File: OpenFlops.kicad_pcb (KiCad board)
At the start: 2 copper layers, 111.6 x 59.4 mm, 87 parts, among them J99 OSHW_LOGO, P1 FLOPPY_CONN, P2 POWER_INPUT, P3 USB_A_FEMALE, P4 PROG_PORT, P5 JUMPER_JC, P6 ENCODER_PORT, P7 DISPLAY_PORT, P8 USB_HEADER, P9 EXTERNAL_SPEAKER, Q1 BSS138, Q2 BSS138, Q3 BSS138, Q4 BSS138, Q5 BSS138, Q6 BSS138, Q7 MMBT3904, U1 74HCT04, U3 STM32F105RBT6, U4 LM1117-3.3, Y1 8 MHz

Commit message: updated to kicad 6; dual mount smt/tht crystal; added test points for swd
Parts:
- added TP2: SWDIO, TestPoint:TestPoint_Pad_D1.0mm, F.Cu at (173.6, 70.9)
- added TP3: SWCLK, TestPoint:TestPoint_Pad_D1.0mm, F.Cu at (173.6, 68.7)
- Y1: footprint Crystal:Crystal_HC49-U_Vertical -> OpenFlops:Crystal_HC49-DualType
- moved Y1 1.97 mm to (154.5, 70.2)
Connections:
- net /~dskchg renamed /~{dskchg}
- net /~dskchg_3v3 renamed /~{dskchg_3v3}
- net /~index renamed /~{index}
- net /~index_3v3 renamed /~{index_3v3}
- net /~inuse renamed /~{inuse}
- net /~mtron renamed /~{mtron}
- net /~rdata renamed /~{rdata}
- net /~rdata_3v3 renamed /~{rdata_3v3}
- net /~rdy renamed /~{rdy}
- net /~rdy_3v3 renamed /~{rdy_3v3}
- net /~sel0 renamed /~{sel0}
- net /~sel1 renamed /~{sel1}
- net /~sel2 renamed /~{sel2}
- net /~selx renamed /~{selx}
- net /~sely renamed /~{sely}
- net /~side renamed /~{side}
- net /~trk0_3v3 renamed /~{trk0_3v3}
- net /~wprot renamed /~{wprot}
- net /~wprot_3v3 renamed /~{wprot_3v3}
- P1 pad 20: /~step -> /dir
- P1 pad 22: /~wdata -> /dir
- P1 pad 24: /~wgate -> /dir
- P1 pad 26: /~trk0 -> /dir
- P1 pad 6: (no net) -> /~{sel3}
- P2 pad 4: (no net) -> unconnected-(P2-Pad4)
- PU6 pad 2: /~step -> /dir
- PU7 pad 2: /~wdata -> /dir
- PU8 pad 2: /~wgate -> /dir
- PU9 pad 2: /~trk0 -> /dir
- Q2 pad 3: /~trk0 -> /dir
- U3 pad 10: (no net) -> unconnected-(U3-Pad10)
- U3 pad 11: (no net) -> unconnected-(U3-Pad11)
- U3 pad 15: /~step -> /dir
- U3 pad 20: (no net) -> unconnected-(U3-Pad20)
- U3 pad 21: (no net) -> unconnected-(U3-Pad21)
- U3 pad 22: (no net) -> unconnected-(U3-Pad22)
- U3 pad 24: (no net) -> unconnected-(U3-Pad24)
- U3 pad 25: (no net) -> unconnected-(U3-Pad25)
- U3 pad 33: (no net) -> /spi_cs
- U3 pad 34: (no net) -> /spi_clk
- U3 pad 35: (no net) -> /spi_do
- U3 pad 36: (no net) -> /spi_di
- U3 pad 40: (no net) -> unconnected-(U3-Pad40)
- U3 pad 41: /~wdata -> /dir
- U3 pad 46: (no net) -> /swdio
- U3 pad 49: (no net) -> /swclk
- U3 pad 54: (no net) -> unconnected-(U3-Pad54)
- U3 pad 62: /~wgate -> /dir
- U3 pad 8: (no net) -> unconnected-(U3-Pad8)
- U3 pad 9: (no net) -> unconnected-(U3-Pad9)
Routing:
- net /dir: track 86.6 -> 436.0 mm, vias 2 -> 7
- net /~wgate: track 106.8 -> 0.00 mm, vias 1 -> 0
- net /~wdata: track 104.9 -> 0.00 mm, vias 1 -> 0
- net /~step: track 78.5 -> 0.00 mm, vias 2 -> 0
- net /~trk0: track 59.3 -> 0.00 mm, vias 1 -> 0
- net /swdio: track 0.00 -> 7.64 mm
- net /swclk: track 0.00 -> 5.27 mm
- net GND: track 0.00 -> 1.52 mm
- net Net-(C5-Pad1): track 15.4 -> 14.5 mm
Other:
- net class Default removed
- net class Power removed
- net class uC removed
- board text added: "SWCLK"
- board text added: "SWDIO"
- board text added: "provided by silvestron.com"

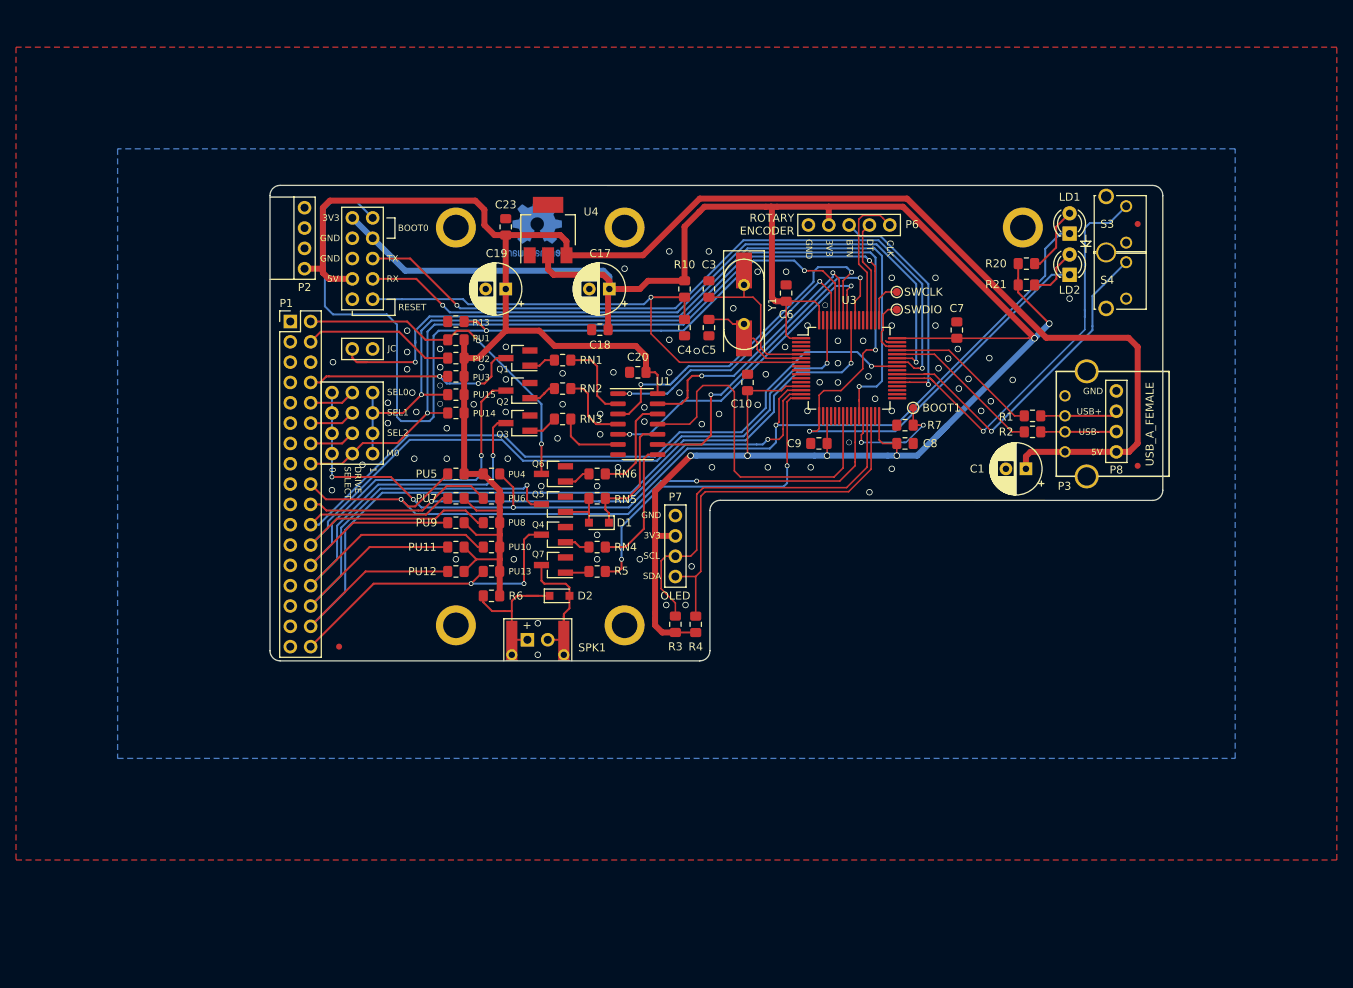
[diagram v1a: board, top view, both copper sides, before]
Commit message: update for citizen w1d
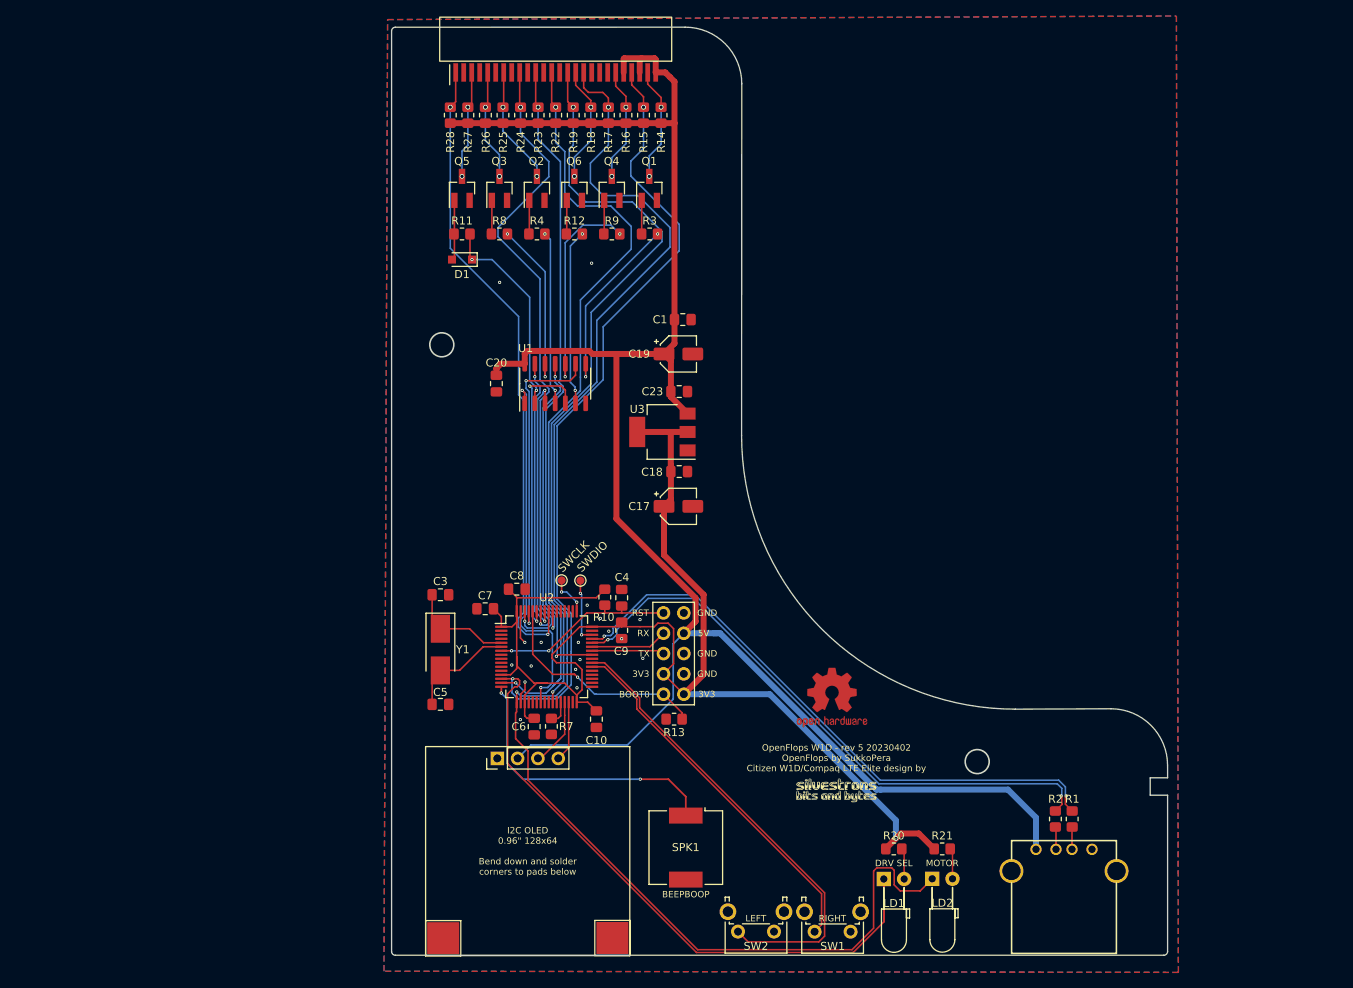
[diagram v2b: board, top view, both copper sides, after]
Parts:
- removed D2: 1N4148, Diode_SMD:D_SOD-323_HandSoldering
- removed FID1, FID2, FID3: Fiducial, Fiducial:Fiducial_0.75mm_Mask1.5mm
- removed H1, H2, H3, H4, H5: MountingHole_Pad, OpenFlops:MountingHole_M3_Pad
- removed P1: FLOPPY_CONN, Connector_PinHeader_2.54mm:PinHeader_2x17_P2.54mm_Vertical
- removed P2: POWER_INPUT, OpenFlops:PinHeader_1x04_P2.54mm_Vertical
- removed P3: USB_A_FEMALE, OpenFlops:USB_A_FEMALE
- removed P4: PROG_PORT, OpenFlops:PinHeader_2x05_P2.54mm_Vertical
- removed P5: JUMPER_JC, OpenFlops:PinHeader_1x02_P2.54mm_Vertical
- removed P6: ENCODER_PORT, OpenFlops:PinHeader_1x05_P2.54mm_Vertical
- removed P7: DISPLAY_PORT, OpenFlops:PinHeader_1x04_P2.54mm_Vertical
- removed P8: USB_HEADER, OpenFlops:PinHeader_1x04_P2.54mm_Vertical
- removed P9: EXTERNAL_SPEAKER, OpenFlops:PinHeader_1x02_P2.54mm_Mute
- removed PA5, PB5, PC5, PD5: Conn_01x03, OpenFlops:PinHeader_1x03_P2.54mm_Mute
- removed PU1, PU10, PU11, PU12, PU13, PU14, PU15, PU2, PU3, PU4, PU5, PU6, PU7, PU8, PU9: 1k, Resistor_SMD:R_0805_2012Metric_Pad1.15x1.40mm_HandSolder
- removed Q7: MMBT3904, Package_TO_SOT_SMD:SOT-23_Handsoldering
- removed R5, RN1, RN2, RN3, RN4, RN5, RN6: 1K, Resistor_SMD:R_0805_2012Metric_Pad1.15x1.40mm_HandSolder
- removed R6: 22, Resistor_SMD:R_0805_2012Metric_Pad1.15x1.40mm_HandSolder
- removed S3: BT_RIGHT, OpenFlops:PUSH_BUTTON_RIGHT_ANGLE
- removed S4: BT_LEFT, OpenFlops:PUSH_BUTTON_RIGHT_ANGLE
- removed TP1: BOOT1, TestPoint:TestPoint_Pad_D1.0mm
- removed U4: LM1117-3.3, Package_TO_SOT_SMD:SOT-223-3_TabPin2
- added J1: FDD, Silvestron Components:Adam_Tech_PCB-C5-26-SA-SMT_1x26_P1.00mm_Horizontal, F.Cu at (131.0, 40.3)
- added J2: USB_A_FEMALE, OpenFlops:USB_A_FEMALE, F.Cu at (194.5, 144.9)
- added J3: PROG_PORT, OpenFlops:PinHeader_2x05_P2.54mm_Vertical, F.Cu at (144.4, 108.8)
- added J4: OLED, Connector_PinHeader_2.54mm:PinHeader_1x04_P2.54mm_Vertical, F.Cu at (123.7, 127.0)
- added J5: OLED Mount, TestPoint:TestPoint_Pad_4.0x4.0mm, F.Cu at (116.9, 149.5)
- added J6: OLED Mount, TestPoint:TestPoint_Pad_4.0x4.0mm, F.Cu at (138.1, 149.4)
- added J7: SBAB_LOGO, Silvestron Components:sbab-tiny-logo, F.Cu at (166.1, 131.0)
- added R11: 1k, Resistor_SMD:R_0805_2012Metric_Pad1.20x1.40mm_HandSolder, F.Cu at (119.3, 61.4)
- added R12: 1k, Resistor_SMD:R_0805_2012Metric_Pad1.20x1.40mm_HandSolder, F.Cu at (133.3, 61.4)
- added R14: 1k, Resistor_SMD:R_0805_2012Metric_Pad1.20x1.40mm_HandSolder, F.Cu at (144.1, 46.6)
- added R15: 1k, Resistor_SMD:R_0805_2012Metric_Pad1.20x1.40mm_HandSolder, F.Cu at (141.9, 46.6)
- added R16: 1k, Resistor_SMD:R_0805_2012Metric_Pad1.20x1.40mm_HandSolder, F.Cu at (139.7, 46.6)
- added R17: 1k, Resistor_SMD:R_0805_2012Metric_Pad1.20x1.40mm_HandSolder, F.Cu at (137.5, 46.6)
- added R18: 1k, Resistor_SMD:R_0805_2012Metric_Pad1.20x1.40mm_HandSolder, F.Cu at (135.4, 46.6)
- added R19: 1k, Resistor_SMD:R_0805_2012Metric_Pad1.20x1.40mm_HandSolder, F.Cu at (133.2, 46.6)
- added R22: 1k, Resistor_SMD:R_0805_2012Metric_Pad1.20x1.40mm_HandSolder, F.Cu at (131.0, 46.6)
- added R23: 1k, Resistor_SMD:R_0805_2012Metric_Pad1.20x1.40mm_HandSolder, F.Cu at (128.8, 46.6)
- added R24: 1k, Resistor_SMD:R_0805_2012Metric_Pad1.20x1.40mm_HandSolder, F.Cu at (126.6, 46.6)
- added R25: 1k, Resistor_SMD:R_0805_2012Metric_Pad1.20x1.40mm_HandSolder, F.Cu at (124.4, 46.6)
- added R26: 1k, Resistor_SMD:R_0805_2012Metric_Pad1.20x1.40mm_HandSolder, F.Cu at (122.2, 46.6)
- added R27: 1k, Resistor_SMD:R_0805_2012Metric_Pad1.20x1.40mm_HandSolder, F.Cu at (120.0, 46.6)
- added R28: 1k, Resistor_SMD:R_0805_2012Metric_Pad1.20x1.40mm_HandSolder, F.Cu at (117.8, 46.6)
- added R8: 1k, Resistor_SMD:R_0805_2012Metric_Pad1.20x1.40mm_HandSolder, F.Cu at (123.9, 61.4)
- added R9: 1k, Resistor_SMD:R_0805_2012Metric_Pad1.20x1.40mm_HandSolder, F.Cu at (138.0, 61.4)
- added SW1: BT_RIGHT, Button_Switch_THT:SW_Tactile_SPST_Angled_PTS645Vx83-2LFS, F.Cu at (167.8, 148.7)
- added SW2: BT_LEFT, Button_Switch_THT:SW_Tactile_SPST_Angled_PTS645Vx83-2LFS, F.Cu at (158.2, 148.7)
- added U2: STM32F105RBT6, Package_QFP:LQFP-64_10x10mm_P0.5mm, F.Cu at (129.8, 114.3)
- C1: value 100u -> 10u; footprint Capacitor_THT:CP_Radial_D6.3mm_P2.50mm -> Capacitor_SMD:C_0805_2012Metric_Pad1.18x1.45mm_HandSolder
- C10, C18, C20, C23, C4, C6, C7, C8, C9: footprint Capacitor_SMD:C_0805_2012Metric_Pad1.15x1.40mm_HandSolder -> Capacitor_SMD:C_0805_2012Metric_Pad1.18x1.45mm_HandSolder
- C17, C19: footprint Capacitor_THT:CP_Radial_D6.3mm_P2.50mm -> Capacitor_SMD:CP_Elec_4x5.4
- C3, C5: value 22p -> 20p; footprint Capacitor_SMD:C_0805_2012Metric_Pad1.15x1.40mm_HandSolder -> Capacitor_SMD:C_0805_2012Metric_Pad1.18x1.45mm_HandSolder
- J99: moved to F.Cu
- LD1, LD2: footprint LED_THT:LED_D3.0mm -> LED_THT:LED_D3.0mm_Horizontal_O3.81mm_Z6.0mm
- R1, R10, R13, R2, R20, R21, R7: footprint Resistor_SMD:R_0805_2012Metric_Pad1.15x1.40mm_HandSolder -> Resistor_SMD:R_0805_2012Metric_Pad1.20x1.40mm_HandSolder
- R3, R4: value 3.3K -> 1k; footprint Resistor_SMD:R_0805_2012Metric_Pad1.15x1.40mm_HandSolder -> Resistor_SMD:R_0805_2012Metric_Pad1.20x1.40mm_HandSolder
- SPK1: footprint OpenFlops:Buzzer -> Buzzer_Beeper:Buzzer_CUI_CPT-9019S-SMT
- U3: value STM32F105RBT6 -> LM1117-3.3; footprint OpenFlops:LQFP-64_Handsoldering -> Package_TO_SOT_SMD:SOT-223-3_TabPin2
- Y1: footprint OpenFlops:Crystal_HC49-DualType -> Crystal:Crystal_SMD_5032-2Pin_5.0x3.2mm_HandSoldering
- moved LD1 83.9 mm to (172.0, 142.1), turned to 0 degrees
- moved LD2 77.4 mm to (178.0, 142.1), turned to 0 degrees
- moved R20 75.0 mm to (173.2, 138.3)
- moved R21 71.3 mm to (179.3, 138.3)
- moved J99 69.2 mm to (165.5, 119.4), turned to 0 degrees
- moved C7 68.5 mm to (122.1, 108.3), turned to 180 degrees
- moved C6 62.7 mm to (128.3, 123.0), turned to -90 degrees
- moved R7 58.1 mm to (130.4, 123.0), turned to 90 degrees
- moved C5 57.8 mm to (116.5, 120.2), turned to 0 degrees
- moved Y1 57.5 mm to (116.5, 113.4)
- moved R13 56.7 mm to (145.8, 122.1)
- moved TP3 55.3 mm to (131.7, 104.8)
- moved R4 52.7 mm to (128.6, 61.4), turned to 0 degrees
- moved TP2 52.1 mm to (134.1, 104.8)
- moved C8 51.8 mm to (126.1, 105.8)
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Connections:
- LD1 pad 1: /~{selx} -> /~{drvs}
- LD2 pad 1: /~{sely} -> /~{mote}
- Q2 pad 3: /dir -> /~{trk00}
- Q3 pad 3: /~{wprot} -> /~{wpt}
- Q4 pad 3: /~{rdy} -> /~{dskchg}
- Q6 pad 3: /~{dskchg} -> /~{redwc}
- R3 pad 1: +3V3 -> Net-(Q1-Pad1)
- R3 pad 2: /disp_clk -> Net-(R3-Pad2)
- R4 pad 1: +3V3 -> Net-(Q2-Pad1)
- R4 pad 2: /disp_dio -> Net-(R4-Pad2)
- SPK1 pad 1: /spk+ -> /jb
- SPK1 pad 2: /spk- -> GND
- U1 pad 1: /~{index_3v3} -> /~{rdata_3v3}
- U1 pad 10: Net-(D1-Pad1) -> Net-(R9-Pad2)
- U1 pad 11: /~{rdata_3v3} -> /~{dskchg_3v3}
- U1 pad 13: /~{dskchg_3v3} -> /~{wprot_3v3}
- U1 pad 2: Net-(RN1-Pad2) -> Net-(D1-Pad1)
- U1 pad 4: Net-(RN2-Pad2) -> Net-(R4-Pad2)
- U1 pad 5: /~{wprot_3v3} -> /~{redwc_3v3}
- U1 pad 8: Net-(RN4-Pad2) -> Net-(R3-Pad2)
- U1 pad 9: /~{rdy_3v3} -> /~{index_3v3}
- U3 pad 1: +3V3 -> GND
- U3 pad 2: GND -> +3V3
- U3 pad 3: GND -> +5V
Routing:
- net /dir: track 436.0 -> 0.00 mm, vias 7 -> 0
- net /~{mote}: track 0.00 -> 183.2 mm, vias 0 -> 2
- net /~{drvs}: track 0.00 -> 180.3 mm, vias 0 -> 2
- net /~{sely}: track 154.9 -> 0.00 mm, vias 3 -> 0
- net /~{selx}: track 133.6 -> 0.00 mm, vias 4 -> 0
- net +3V3: track 288.7 -> 172.7 mm, vias 6 -> 1
- net /jc: track 99.9 -> 0.00 mm, vias 2 -> 0
- net /~{mtron}: track 97.4 -> 0.00 mm, vias 2 -> 0
- net /~{step}: track 0.00 -> 97.2 mm, vias 0 -> 2
- net /~{dir}: track 0.00 -> 94.5 mm, vias 0 -> 2
- net /boot0: track 119.5 -> 28.6 mm, vias 2 -> 1
- net /~{wgate}: track 0.00 -> 82.2 mm, vias 0 -> 2
- net /tx: track 91.1 -> 9.06 mm, vias 2 -> 0
- net /~{wdate}: track 0.00 -> 80.7 mm, vias 0 -> 2
- net /rx: track 87.9 -> 9.61 mm, vias 2 -> 0
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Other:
- board size 111.6 x 59.4 mm -> 97 x 116 mm
- board text added: "BEEPBOOP"
- board text added: "DRV SEL"
- board text added: "I2C OLED 0.96{dblquote} 128x64 Bend down and solder corners to pads below"
- board text added: "LEFT"
- board text added: "MOTOR"
- board text added: "OpenFlops W1D - rev 5 20230402 OpenFlops by SukkoPera Citizen W1D/Compaq LTE Elite design by"
- board text added: "RIGHT"
- board text added: "RST"
- board text added: "Your files go through these wires"
- board text removed: "+"
- board text removed: "0"
- board text removed: "1"
- board text removed: "BOOT1"
- board text removed: "BTN"
- board text removed: "CLK"
- board text removed: "DRIVE SELECT"
- board text removed: "DT"
- board text removed: "JC"
- board text removed: "Licensed under CERN OHL v.1.2"
- board text removed: "M0"
- board text removed: "OLED"
- board text removed: "RESET"
- board text removed: "ROTARY ENCODER"
- board text removed: "SCL"
- board text removed: "SDA"
- board text removed: "SEL0"
- board text removed: "SEL1"
- board text removed: "SEL2"
- board text removed: "USB+"
- board text removed: "USB-"
- board text removed: "V1"
- board text removed: "github.com/SukkoPera/OpenFlops"
- board text removed: "provided by silvestron.com"

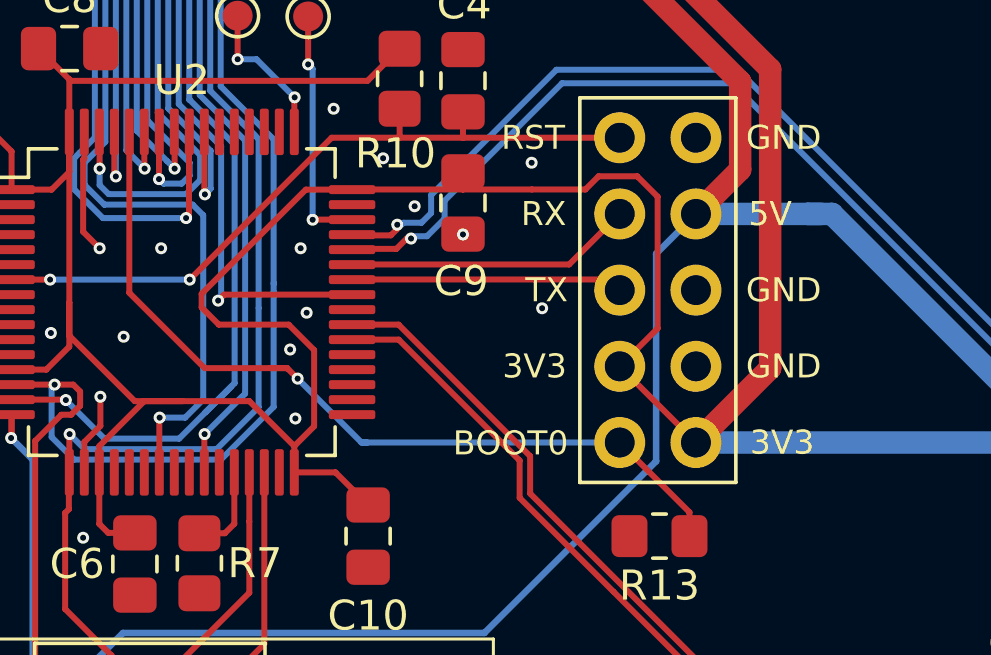
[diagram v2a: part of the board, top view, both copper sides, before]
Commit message: updating to fix a few cut ground traces
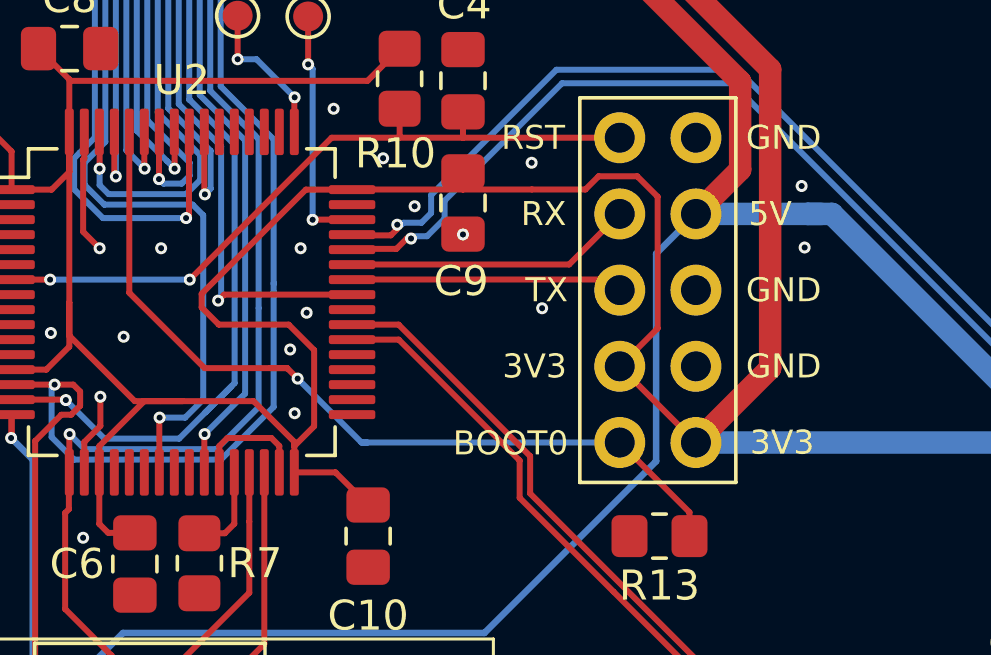
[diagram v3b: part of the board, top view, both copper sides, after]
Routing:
- net GND: track 6.87 -> 10.8 mm, vias 18 -> 20
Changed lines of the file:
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@@
   (segment (start 126.589399 108.620673) (end 126.589399 109.510601) (width 0.2) (layer "F.Cu") (net 1))
   (segment (start 126.55 111.95) (end 127.1 112.5) (width 0.2) (layer "F.Cu") (net 1))
+  (segment (start 132.825 118.825) (end 131.358751 118.825) (width 0.2) (layer "F.Cu") (net 1))
   (segment (start 126.589399 119.970673) (end 126.589399 118.959595) (width 0.2) (layer "F.Cu") (net 1))
   (segment (start 126.589399 118.959595) (end 127.125 118.423994) (width 0.2) (layer "F.Cu") (net 1))
   (segment (start 126.589399 109.510601) (end 126.55 109.55) (width 0.2) (layer "F.Cu") (net 1))
   (segment (start 127.125 118.423994) (end 127.125 117.45) (width 0.2) (layer "F.Cu") (net 1))
+  (segment (start 133.089399 119.970673) (end 133.089399 119.089399) (width 0.2) (layer "F.Cu") (net 1))
+  (segment (start 133.089399 119.089399) (end 132.825 118.825) (width 0.2) (layer "F.Cu") (net 1))
+  (segment (start 131.358751 118.825) (end 131.089399 119.094352) (width 0.2) (layer "F.Cu") (net 1))
   (segment (start 126.55 109.55) (end 126.55 111.95) (width 0.2) (layer "F.Cu") (net 1))
+  (segment (start 131.089399 119.094352) (end 131.089399 119.970673) (width 0.2) (layer "F.Cu") (net 1))
+  (via (at 150.6 112.475) (size 0.4) (drill 0.2) (layers "F.Cu" "B.Cu") (free) (net 1))
   (via (at 135.45 65.1) (size 0.4) (drill 0.2) (layers "F.Cu" "B.Cu") (free) (net 1))
   (via (at 134 114.65) (size 0.4) (drill 0.2) (layers "F.Cu" "B.Cu") (free) (net 1))
@@
   (via (at 133.45 115.875) (size 0.4) (drill 0.2) (layers "F.Cu" "B.Cu") (free) (net 1))
   (via (at 139.211649 112.040675) (size 0.4) (drill 0.2) (layers "F.Cu" "B.Cu") (net 1))
-  (via (at 133.625 118.175) (size 0.4) (drill 0.2) (layers "F.Cu" "B.Cu") (free) (net 1))
+  (via (at 133.6 118) (size 0.4) (drill 0.2) (layers "F.Cu" "B.Cu") (free) (net 1))
   (via (at 127.9 115.45) (size 0.4) (drill 0.2) (layers "F.Cu" "B.Cu") (free) (net 1))
   (via (at 137.6 111.1) (size 0.4) (drill 0.2) (layers "F.Cu" "B.Cu") (free) (net 1))
@@
   (via (at 141.85 114.5) (size 0.4) (drill 0.2) (layers "F.Cu" "B.Cu") (free) (net 1))
   (via (at 127.1 112.5) (size 0.4) (drill 0.2) (layers "F.Cu" "B.Cu") (free) (net 1))
+  (via (at 150.5 110.425) (size 0.4) (drill 0.2) (layers "F.Cu" "B.Cu") (free) (net 1))
   (via (at 134.9 107.85) (size 0.4) (drill 0.2) (layers "F.Cu" "B.Cu") (free) (net 1))
   (via (at 136.55 109.5) (size 0.4) (drill 0.2) (layers "F.Cu" "B.Cu") (free) (net 1))
@@
   (segment (start 145.362501 91.145673) (end 145.362501 94.633173) (width 0.75) (layer "F.Cu") (net 5))
   (segment (start 128.269036 117.596163) (end 128.546163 117.596163) (width 0.2) (layer "F.Cu") (net 5))
-  (segment (start 130.549012 117.596163) (end 129.878837 117.596163) (width 0.2) (layer "F.Cu") (net 5))
   (segment (start 144.500001 101.582139) (end 149.450679 106.532817) (width 0.75) (layer "F.Cu") (net 5))
   (segment (start 130.49999 114.472789) (end 130.49999 114.018557) (width 0.2) (layer "F.Cu") (net 5))
@@
   (segment (start 127.3875 121.9875) (end 128.275 121.9875) (width 0.2) (layer "F.Cu") (net 5))
   (segment (start 144.500001 95.495673) (end 144.500001 101.582139) (width 0.75) (layer "F.Cu") (net 5))
+  (segment (start 132.231881 117.596163) (end 129.878837 117.596163) (width 0.2) (layer "F.Cu") (net 5))
   (segment (start 125.499501 110.545673) (end 126.0894 109.955774) (width 0.2) (layer "F.Cu") (net 5))
   (segment (start 126.0894 114.3106) (end 126.0894 108.620674) (width 0.2) (layer "F.Cu") (net 5))
-  (segment (start 133.589399 119.095313) (end 132.09025 117.596162) (width 0.2) (layer "F.Cu") (net 5))
   (segment (start 128.546163 117.596163) (end 129.121163 117.596163) (width 0.2) (layer "F.Cu") (net 5))
   (segment (start 176.35 136.387501) (end 178.275 138.312501) (width 0.75) (layer "F.Cu") (net 5))
@@
   (segment (start 124.164401 109.273073) (end 123.187001 108.295673) (width 0.2) (layer "F.Cu") (net 5))
   (segment (start 145.7 110.781679) (end 145.7 115.172321) (width 0.2) (layer "F.Cu") (net 5))
-  (segment (start 132.09025 117.596162) (end 130.549012 117.596163) (width 0.2) (layer "F.Cu") (net 5))
   (segment (start 126.0894 109.955774) (end 126.0894 108.620674) (width 0.2) (layer "F.Cu") (net 5))
   (segment (start 127.089399 119.970673) (end 127.089399 121.689399) (width 0.2) (layer "F.Cu") (net 5))
@@
   (segment (start 133.5894 119.970673) (end 133.589399 119.095313) (width 0.2) (layer "F.Cu") (net 5))
   (segment (start 145.350001 86.195674) (end 145.350001 90.295673) (width 0.75) (layer "F.Cu") (net 5))
+  (segment (start 133.589399 118.953681) (end 132.231881 117.596163) (width 0.2) (layer "F.Cu") (net 5))
   (segment (start 124.164401 110.545673) (end 124.164401 109.273073) (width 0.2) (layer "F.Cu") (net 5))
   (segment (start 141.150001 86.195674) (end 144.250001 86.195672) (width 0.75) (layer "F.Cu") (net 5))
@@
   (segment (start 145.350001 90.295673) (end 145.350001 91.133173) (width 0.75) (layer "F.Cu") (net 5))
   (segment (start 126.0894 115.778646) (end 126.0894 114.3106) (width 0.2) (layer "F.Cu") (net 5))
+  (segment (start 133.589399 119.095313) (end 133.589399 118.953681) (width 0.2) (layer "F.Cu") (net 5))
   (segment (start 143.733301 110.1) (end 145.018321 110.1) (width 0.2) (layer "F.Cu") (net 5))
   (segment (start 124.164401 110.545673) (end 125.499501 110.545673) (width 0.2) (layer "F.Cu") (net 5))
